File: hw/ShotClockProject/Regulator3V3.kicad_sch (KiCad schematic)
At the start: 12 parts, among them U2 TPS63000

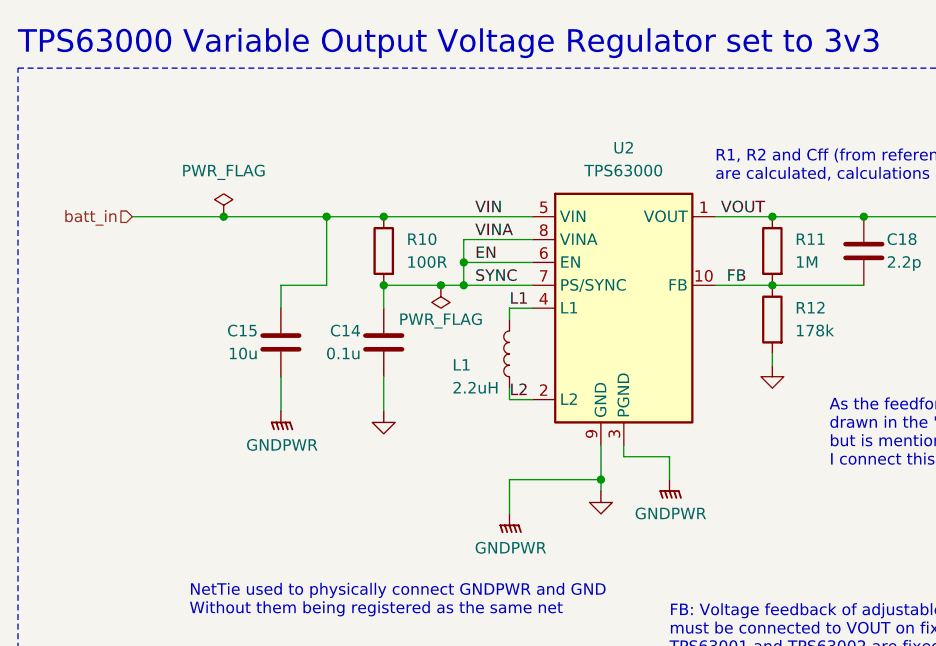
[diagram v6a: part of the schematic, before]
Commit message: Routing on mainboard for LiPo charger
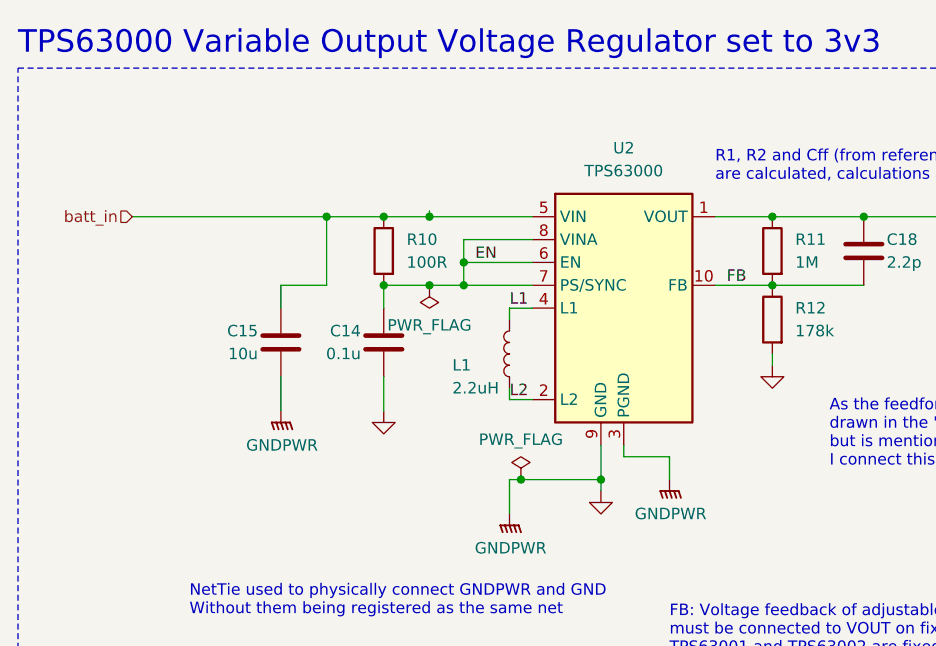
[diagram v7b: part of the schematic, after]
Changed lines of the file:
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@@
   (junction (at 59.69 38.1) (diameter 0) (color 0 0 0 0)
   )
+  (junction (at 64.77 38.1) (diameter 0) (color 0 0 0 0)
+  )
   (junction (at 68.58 43.18) (diameter 0) (color 0 0 0 0)
   )
-  (junction (at 66.04 45.72) (diameter 0) (color 0 0 0 0)
-  )
   (junction (at 59.69 45.72) (diameter 0) (color 0 0 0 0)
   )
-  (junction (at 41.91 38.1) (diameter 0) (color 0 0 0 0)
-  )
   (junction (at 53.34 38.1) (diameter 0) (color 0 0 0 0)
   )
@@
   (junction (at 68.58 45.72) (diameter 0) (color 0 0 0 0)
   )
+  (junction (at 64.77 45.72) (diameter 0) (color 0 0 0 0)
+  )
   (junction (at 139.7 40.64) (diameter 0) (color 0 0 0 0)
   )
+  (junction (at 74.93 67.31) (diameter 0) (color 0 0 0 0)
+  )
   (wire (pts (xy 113.03 45.72) (xy 102.87 45.72))
     (stroke (width 0) (type default))
@@
     (stroke (width 0) (type default))
   )
-  (wire (pts (xy 66.04 45.72) (xy 68.58 45.72))
+  (wire (pts (xy 59.69 45.72) (xy 64.77 45.72))
     (stroke (width 0) (type default))
   )
@@
     (stroke (width 0) (type default))
   )
-  (wire (pts (xy 59.69 38.1) (xy 76.2 38.1))
+  (wire (pts (xy 59.69 38.1) (xy 64.77 38.1))
+    (stroke (width 0) (type default))
+  )
+  (wire (pts (xy 74.93 67.31) (xy 83.82 67.31))
+    (stroke (width 0) (type default))
+  )
+  (wire (pts (xy 64.77 37.465) (xy 64.77 38.1))
     (stroke (width 0) (type default))
   )
@@
     (stroke (width 0) (type default))
   )
-  (wire (pts (xy 73.66 67.31) (xy 83.82 67.31))
+  (wire (pts (xy 73.66 67.31) (xy 74.93 67.31))
+    (stroke (width 0) (type default))
+  )
+  (wire (pts (xy 154.94 38.1) (xy 172.72 38.1))
+    (stroke (width 0) (type default))
+  )
+  (wire (pts (xy 113.03 38.1) (xy 139.7 38.1))
+    (stroke (width 0) (type default))
+  )
+  (wire (pts (xy 68.58 40.64) (xy 76.2 40.64))
+    (stroke (width 0) (type default))
+  )
+  (wire (pts (xy 48.26 48.26) (xy 48.26 45.72))
+    (stroke (width 0) (type default))
+  )
+  (wire (pts (xy 76.2 58.42) (xy 73.66 58.42))
+    (stroke (width 0) (type default))
+  )
+  (wire (pts (xy 83.82 67.31) (xy 83.82 68.58))
     (stroke (width 0) (type default))
   )
@@
     (stroke (width 0) (type default))
   )
-  (wire (pts (xy 154.94 38.1) (xy 172.72 38.1))
-    (stroke (width 0) (type default))
-  )
-  (wire (pts (xy 113.03 38.1) (xy 139.7 38.1))
-    (stroke (width 0) (type default))
-  )
-  (wire (pts (xy 68.58 40.64) (xy 76.2 40.64))
-    (stroke (width 0) (type default))
-  )
-  (wire (pts (xy 48.26 48.26) (xy 48.26 45.72))
-    (stroke (width 0) (type default))
-  )
-  (wire (pts (xy 76.2 58.42) (xy 73.66 58.42))
-    (stroke (width 0) (type default))
-  )
-  (wire (pts (xy 83.82 67.31) (xy 83.82 68.58))
+  (wire (pts (xy 64.77 45.72) (xy 68.58 45.72))
     (stroke (width 0) (type default))
   )
@@
     (stroke (width 0) (type default))
   )
-  (wire (pts (xy 41.91 38.1) (xy 53.34 38.1))
+  (wire (pts (xy 31.75 38.1) (xy 53.34 38.1))
     (stroke (width 0) (type default))
   )
@@
     (stroke (width 0) (type default))
   )
-  (wire (pts (xy 59.69 45.72) (xy 66.04 45.72))
+  (wire (pts (xy 64.77 38.1) (xy 76.2 38.1))
     (stroke (width 0) (type default))
   )
   (wire (pts (xy 73.66 58.42) (xy 73.66 57.15))
-    (stroke (width 0) (type default))
-  )
-  (wire (pts (xy 31.75 38.1) (xy 41.91 38.1))
     (stroke (width 0) (type default))
   )
@@
     (effects (font (size 2.5 2.5) (color 255 0 0 1)) (justify left bottom))
   )
-  (label "VOUT" (at 97.155 38.1 0) (fields_autoplaced)
-    (effects (font (size 1.27 1.27)) (justify left bottom))
-  )
-  (label "VIN" (at 69.85 38.1 0) (fields_autoplaced)
-    (effects (font (size 1.27 1.27)) (justify left bottom))
-  )
-  (label "VINA" (at 69.85 40.64 0) (fields_autoplaced)
-    (effects (font (size 1.27 1.27)) (justify left bottom))
-  )
   (label "FB" (at 97.79 45.72 0) (fields_autoplaced)
     (effects (font (size 1.27 1.27)) (justify left bottom))
@@
   )
   (label "EN" (at 69.85 43.18 0) (fields_autoplaced)
-    (effects (font (size 1.27 1.27)) (justify left bottom))
-  )
-  (label "SYNC" (at 69.85 45.72 0) (fields_autoplaced)
     (effects (font (size 1.27 1.27)) (justify left bottom))
   )
@@
     )
   )
+  (symbol (lib_id "power:PWR_FLAG") (at 74.93 67.31 0) (unit 1)
+    (in_bom yes) (on_board yes) (dnp no)
+    (property "Reference" "#FLG03" (at 74.93 65.405 0)
+      (effects (font (size 1.27 1.27)) hide)
+    )
+    (property "Value" "PWR_FLAG" (at 74.93 62.865 0)
+      (effects (font (size 1.27 1.27)))
+    )
+    (property "Footprint" "" (at 74.93 67.31 0)
+      (effects (font (size 1.27 1.27)) hide)
+    )
+    (property "Datasheet" "~" (at 74.93 67.31 0)
+      (effects (font (size 1.27 1.27)) hide)
+    )
+    (pin "1")
+    (instances
+      (project "ShotClockProject"
+        (path "/5fd859aa-754d-49c2-9762-3f7ebe3bb64c/d287d155-1951-4d4f-8d6c-570f03bc79f5"
+          (reference "#FLG03") (unit 1)
+        )
+        (path "/5fd859aa-754d-49c2-9762-3f7ebe3bb64c/17367eb9-0f4d-4017-b1ca-d50430410a5d"
+          (reference "#FLG010") (unit 1)
+        )
+        (path "/5fd859aa-754d-49c2-9762-3f7ebe3bb64c"
+          (reference "#FLG09") (unit 1)
+        )
+      )
+    )
+  )
   (symbol (lib_id "Device:LED") (at 154.94 45.72 270) (mirror x) (unit 1)
     (in_bom yes) (on_board yes) (dnp no)
@@
     )
   )
-  (symbol (lib_id "power:PWR_FLAG") (at 41.91 38.1 0) (unit 1)
-    (in_bom yes) (on_board yes) (dnp no) (fields_autoplaced)
-    (property "Reference" "#FLG04" (at 41.91 36.195 0)
-      (effects (font (size 1.27 1.27)) hide)
-    )
-    (property "Value" "PWR_FLAG" (at 41.91 33.02 0)
-      (effects (font (size 1.27 1.27)))
-    )
-    (property "Footprint" "" (at 41.91 38.1 0)
-      (effects (font (size 1.27 1.27)) hide)
-    )
-    (property "Datasheet" "~" (at 41.91 38.1 0)
-      (effects (font (size 1.27 1.27)) hide)
-    )
-    (pin "1")
-    (instances
-      (project "ShotClockProject"
-        (path "/5fd859aa-754d-49c2-9762-3f7ebe3bb64c/d287d155-1951-4d4f-8d6c-570f03bc79f5"
-          (reference "#FLG04") (unit 1)
-        )
-        (path "/5fd859aa-754d-49c2-9762-3f7ebe3bb64c/17367eb9-0f4d-4017-b1ca-d50430410a5d"
-          (reference "#FLG06") (unit 1)
-        )
-        (path "/5fd859aa-754d-49c2-9762-3f7ebe3bb64c/83d8d19c-1376-4688-800d-ae057ad1fe11"
-          (reference "#FLG010") (unit 1)
-        )
-      )
-    )
-  )
   (symbol (lib_id "Device:C") (at 134.62 44.45 0) (mirror y) (unit 1)
     (in_bom yes) (on_board yes) (dnp no)
@@
     )
   )
+  (symbol (lib_id "power:PWR_FLAG") (at 64.77 45.72 180) (unit 1)
+    (in_bom yes) (on_board yes) (dnp no) (fields_autoplaced)
+    (property "Reference" "#FLG03" (at 64.77 47.625 0)
+      (effects (font (size 1.27 1.27)) hide)
+    )
+    (property "Value" "PWR_FLAG" (at 64.77 50.165 0)
+      (effects (font (size 1.27 1.27)))
+    )
+    (property "Footprint" "" (at 64.77 45.72 0)
+      (effects (font (size 1.27 1.27)) hide)
+    )
+    (property "Datasheet" "~" (at 64.77 45.72 0)
+      (effects (font (size 1.27 1.27)) hide)
+    )
+    (pin "1")
+    (instances
+      (project "ShotClockProject"
+        (path "/5fd859aa-754d-49c2-9762-3f7ebe3bb64c/d287d155-1951-4d4f-8d6c-570f03bc79f5"
+          (reference "#FLG03") (unit 1)
+        )
+        (path "/5fd859aa-754d-49c2-9762-3f7ebe3bb64c/17367eb9-0f4d-4017-b1ca-d50430410a5d"
+          (reference "#FLG04") (unit 1)
+        )
+      )
+    )
+  )
   (symbol (lib_id "Device:C") (at 113.03 41.91 0) (unit 1)
     (in_bom yes) (on_board yes) (dnp no)
@@
         )
       )
-    )
-  )
-  (symbol (lib_id "power:PWR_FLAG") (at 66.04 45.72 180) (unit 1)
-    (in_bom yes) (on_board yes) (dnp no)
-    (property "Reference" "#FLG04" (at 66.04 47.625 0)
-      (effects (font (size 1.27 1.27)) hide)
-    )
-    (property "Value" "PWR_FLAG" (at 66.04 49.53 0)
-      (effects (font (size 1.27 1.27)))
-    )
-    (property "Footprint" "" (at 66.04 45.72 0)
-      (effects (font (size 1.27 1.27)) hide)
-    )
-    (property "Datasheet" "~" (at 66.04 45.72 0)
-      (effects (font (size 1.27 1.27)) hide)
-    )
-    (pin "1")
-    (instances
-      (project "ShotClockProject"
-        (path "/5fd859aa-754d-49c2-9762-3f7ebe3bb64c/d287d155-1951-4d4f-8d6c-570f03bc79f5"
-          (reference "#FLG04") (unit 1)
-        )
-        (path "/5fd859aa-754d-49c2-9762-3f7ebe3bb64c/17367eb9-0f4d-4017-b1ca-d50430410a5d"
-          (reference "#FLG07") (unit 1)
-        )
-        (path "/5fd859aa-754d-49c2-9762-3f7ebe3bb64c/83d8d19c-1376-4688-800d-ae057ad1fe11"
-          (reference "#FLG011") (unit 1)
-        )
-      )

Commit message: Finished routing and added silk + part nmbr
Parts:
- C14: LCSC Part # C1525 -> (none)
- C15, C16, C17: LCSC Part # C96446 -> (none)
- C18: LCSC Part # C1559 -> (none)
- D2: LCSC Part # C72043 -> (none)
- L1: LCSC Part # C404494 -> (none)
- R10: LCSC Part # C25867 -> (none)
- R10: LCSC Part # C25076 -> (none)
- R11: LCSC Part # C144787 -> (none)
- R12: LCSC Part # C185459 -> (none)
- U2: LCSC Part # C24966 -> (none)
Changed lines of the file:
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@@
       (effects (font (size 1.27 1.27)) hide)
     )
-    (property "LCSC Part #" "C25867" (at 154.94 54.61 0)
+    (property "LCSC Part #" "" (at 154.94 54.61 0)
       (effects (font (size 1.27 1.27)) hide)
     )
@@
       (effects (font (size 1.27 1.27)) hide)
     )
-    (property "LCSC Part #" "C96446" (at 144.78 44.45 0)
+    (property "LCSC Part #" "" (at 144.78 44.45 0)
       (effects (font (size 1.27 1.27)) hide)
     )
@@
       (effects (font (size 1.27 1.27)) hide)
     )
-    (property "LCSC Part #" "C1525" (at 59.69 52.07 0)
+    (property "LCSC Part #" "" (at 59.69 52.07 0)
       (effects (font (size 1.27 1.27)) hide)
     )
@@
       (effects (font (size 1.27 1.27)) hide)
     )
-    (property "LCSC Part #" "C144787" (at 102.87 41.91 0)
+    (property "LCSC Part #" "" (at 102.87 41.91 0)
       (effects (font (size 1.27 1.27)) hide)
     )
@@
       (effects (font (size 1.27 1.27)) hide)
     )
-    (property "LCSC Part #" "C96446" (at 48.26 52.07 0)
+    (property "LCSC Part #" "" (at 48.26 52.07 0)
       (effects (font (size 1.27 1.27)) hide)
     )
@@
       (effects (font (size 1.27 1.27)) hide)
     )
-    (property "LCSC Part #" "C24966" (at 86.36 48.26 0)
+    (property "LCSC Part #" "" (at 86.36 48.26 0)
       (effects (font (size 1.27 1.27)) hide)
     )
@@
       (effects (font (size 1.27 1.27)) hide)
     )
-    (property "LCSC Part #" "C72043" (at 154.94 45.72 0)
+    (property "LCSC Part #" "" (at 154.94 45.72 0)
       (effects (font (size 1.27 1.27)) hide)
     )
@@
       (effects (font (size 1.27 1.27)) hide)
     )
-    (property "LCSC Part #" "C96446" (at 134.62 44.45 0)
+    (property "LCSC Part #" "" (at 134.62 44.45 0)
       (effects (font (size 1.27 1.27)) hide)
     )
@@
       (effects (font (size 1.27 1.27)) hide)
     )
-    (property "LCSC Part #" "C185459" (at 102.87 49.53 0)
+    (property "LCSC Part #" "" (at 102.87 49.53 0)
       (effects (font (size 1.27 1.27)) hide)
     )
@@
       (effects (font (size 1.27 1.27)) hide)
     )
-    (property "LCSC Part #" "C1559" (at 113.03 41.91 0)
+    (property "LCSC Part #" "" (at 113.03 41.91 0)
       (effects (font (size 1.27 1.27)) hide)
     )
@@
       (effects (font (size 1.27 1.27)) hide)
     )
-    (property "LCSC Part #" "C25076" (at 59.69 41.91 0)
+    (property "LCSC Part #" "" (at 59.69 41.91 0)
       (effects (font (size 1.27 1.27)) hide)
     )
@@
       (effects (font (size 1.27 1.27)) hide)
     )
-    (property "LCSC Part #" "C404494" (at 73.66 53.34 0)
-      (effects (font (size 1.27 1.27)) hide)
-    )
+    (property "LCSC Part #" "" (at 73.66 53.34 0)
+      (effects (font (size 1.27 1.27)) hide)
+    )
